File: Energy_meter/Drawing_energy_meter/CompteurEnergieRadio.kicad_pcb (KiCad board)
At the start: 2 copper layers, 33 x 95.3 mm, 7 parts, among them J1 Power, J2 Puissance PZEM, J3 Serie PZEM, P1 Alimentation230/5, U1 NRF24L01_Breakout, U2 OLED_I2C_128X64_096IN

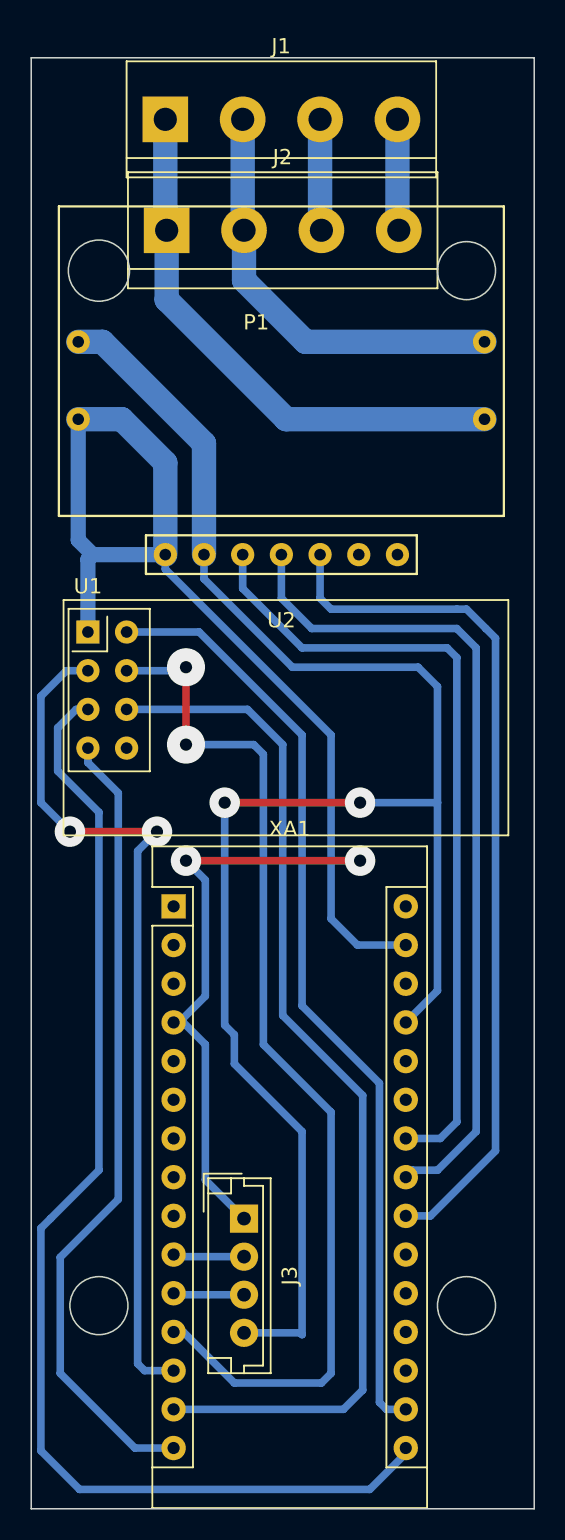
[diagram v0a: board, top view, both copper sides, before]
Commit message: Correction on PCB and add cover stl file
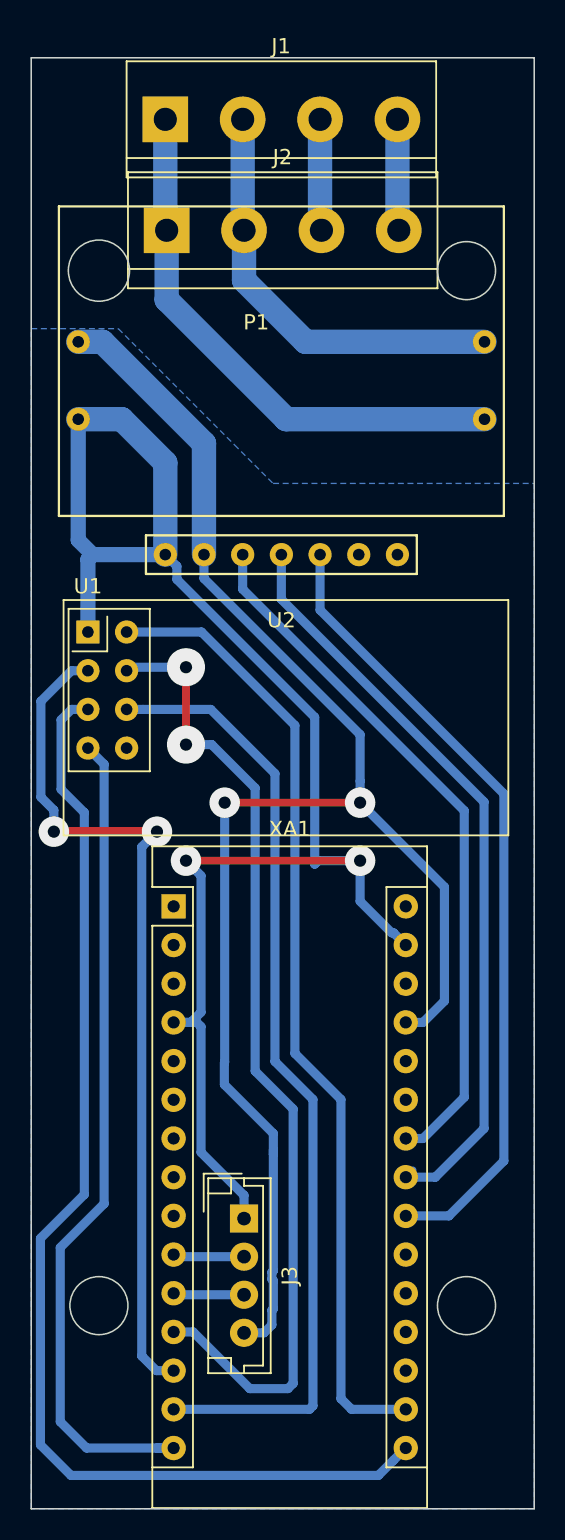
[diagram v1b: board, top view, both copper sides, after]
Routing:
- net +5V: track 115.9 -> 104.3 mm
- net Net-(U2-Pad3): track 52.4 -> 46.6 mm
- net Net-(U1-Pad6): track 68.7 -> 63.3 mm
- net Net-(U2-Pad4): track 54.6 -> 50.3 mm
- net Net-(U2-Pad5): track 56.8 -> 52.7 mm
- net Net-(U1-Pad4): track 68.9 -> 65.4 mm
- net Net-(U1-Pad7): track 52.9 -> 55.1 mm
- net Net-(U1-Pad5): track 79.0 -> 77.4 mm
- net +3V3: track 62.2 -> 63.6 mm
- net GND: track 106.9 -> 106.0 mm
- added copper zone on B.Cu, net GND
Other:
- net class Default: clearance 0.6 -> 0.7; trace_width 0.5 -> 0.6
- rule trace_clearance: 0.6 -> 0.7
